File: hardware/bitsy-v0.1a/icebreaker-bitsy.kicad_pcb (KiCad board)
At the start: 4 copper layers, 38.1 x 17.8 mm, 93 parts, among them J1 Conn_01x01, J10 Conn_01x01, J11 Conn_01x01, J12 Conn_01x01, J13 Conn_01x01, J14 Jumper, J15 Jumper, J16 Jumper, J17 Jumper, J18 Jumper, J19 Jumper, J2 Conn_01x01, J20 Conn_01x01, J21 Conn_01x01, J22 Conn_01x01, J23 Conn_01x01, J24 Conn_01x01, J25 Conn_01x01, J26 Conn_01x01, J27 Conn_01x01, J28 Conn_01x01, J29 Conn_01x01, J3 Conn_01x01, J30 Conn_01x01, J31 Conn_01x01, J32 Conn_01x01, J33 Conn_01x01, J34 Conn_01x01, J35 Conn_01x01, J36 Conn_01x01, J37 Conn_01x01, J4 Conn_01x01, J41 Conn_01x01, J42 Conn_01x01, J43 Conn_01x01, J44 Conn_01x01, J45 Conn_01x01, J46 Conn_01x01, J47 Conn_01x01, J48 Conn_01x01, J49 Conn_01x01, J5 Conn_01x01, J6 Conn_01x01, J7 Conn_01x01, J8 Conn_01x01, J9 Conn_01x01, P1 pkl_USB_OTG, SW1 TACT, U2 3.3V, U3 1V2, U5 W25Q, U6 ICE5LP4K-SG48, X1 12MHz

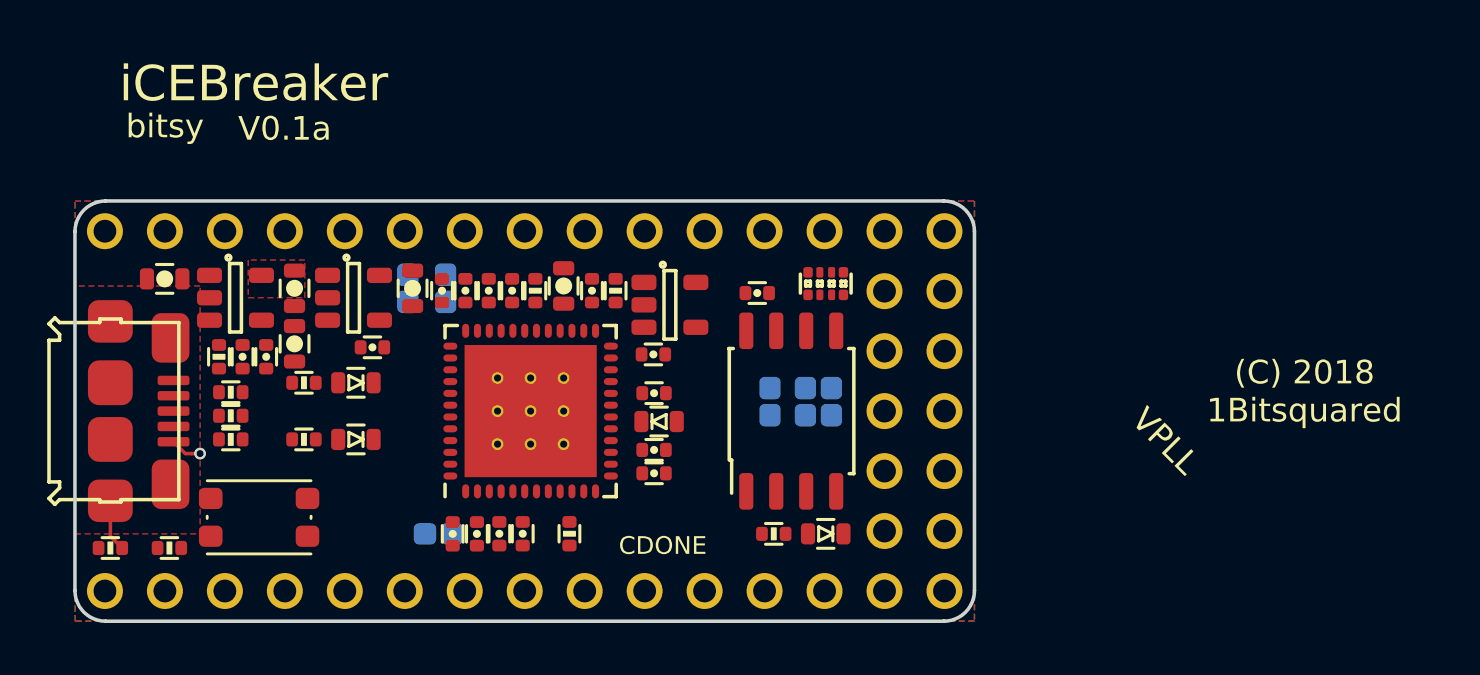
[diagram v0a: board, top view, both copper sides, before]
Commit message: Schematic cleanup and minor improvements.
Added ESD protection on the USB interface, added +5V VIN Jumper.
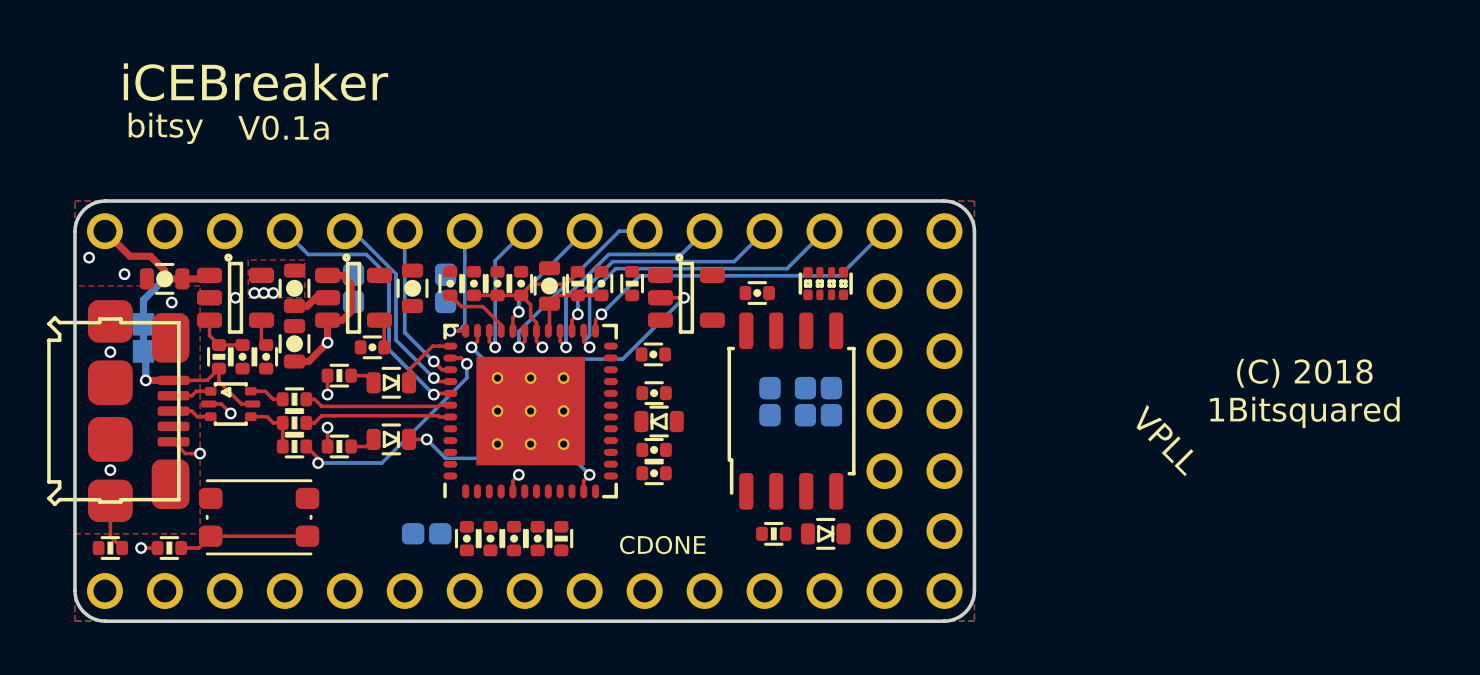
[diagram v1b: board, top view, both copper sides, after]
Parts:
- added J38: Jumper, pkl_jumpers:J_0603, B.Cu at (32.9, 44.4)
- added U1: USBLC6-2, pkl_housings_sot:SOT-666, F.Cu at (36.6, 47.2)
- P1: value pkl_USB_OTG -> USB_OTG
- moved R2 2.72 mm to (39.3, 49.0)
- moved R4 2.72 mm to (39.3, 47.0)
- moved R6 2.72 mm to (39.3, 48.0)
- moved J14 2.30 mm to (41.8, 42.3)
- moved R10 1.82 mm to (51.3, 42.1)
- moved R14 1.53 mm to (41.2, 46.0)
- moved R15 1.53 mm to (41.2, 49.0)
- moved D4 1.50 mm to (43.4, 46.3)
- moved D5 1.50 mm to (43.4, 48.7)
- moved R7 0.76 mm to (53.6, 42.1)
- moved X1 0.76 mm to (55.9, 42.7)
- moved C36 0.67 mm to (49.6, 52.9)
- moved C37 0.66 mm to (48.6, 52.9)
- moved C27 0.63 mm to (46.6, 52.9)
- moved C38 0.61 mm to (47.6, 52.9)
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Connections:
- R2 pad 2: /xUD+ -> /iUD+
- R4 pad 2: /xUD- -> /iUD-
- R6 pad 2: /xUD+ -> /iUD+
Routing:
- net +5V: track 0.00 -> 29.7 mm, vias 0 -> 3
- net /IOT_39A: track 0.00 -> 14.3 mm, vias 0 -> 1
- net /IOT_36b: track 0.00 -> 14.3 mm, vias 0 -> 1
- net /CLK: track 0.00 -> 12.1 mm, vias 0 -> 2
- net /~LED_BLU: track 0.00 -> 11.7 mm, vias 0 -> 1
- net /IOT_38B: track 0.00 -> 10.6 mm, vias 0 -> 1
- net /USB_DET: track 0.00 -> 10.1 mm, vias 0 -> 2
- net /IOT_41A: track 0.00 -> 9.96 mm, vias 0 -> 1
- net /~LEDR: track 0.00 -> 9.07 mm, vias 0 -> 2
- net /~LED_GRN: track 0.00 -> 8.75 mm, vias 0 -> 1
- net /IOT_42B: track 0.00 -> 8.56 mm, vias 0 -> 1
- net +1V2: track 0.00 -> 8.19 mm, vias 0 -> 2
- net /~LED_RED: track 0.00 -> 6.87 mm, vias 0 -> 1
- net /IOT_44B: track 0.00 -> 6.42 mm, vias 0 -> 1
- net /USB_P: track 0.00 -> 6.24 mm
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- added copper zone on In2.Cu, net +1V2
- added copper zone on In1.Cu, net /shield

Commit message: First shot at fully routing the board! :D
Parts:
- moved REF** 45.2 mm to (41.6, 47.4), turned to 90 degrees
- moved C31 5.34 mm to (54.8, 44.8)
- moved C4 2.22 mm to (56.7, 44.8)
- moved C29 0.98 mm to (54.8, 48.2)
- moved C35 0.98 mm to (54.8, 45.8)
- moved D2 0.98 mm to (55.0, 47.0)
- moved R11 0.81 mm to (61.0, 42.0)
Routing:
- net +3V3: track 5.22 -> 41.4 mm, vias 7 -> 19
- net /FLASH_MISO/IO1: track 0.00 -> 24.9 mm, vias 0 -> 3
- net /FLASH_~WP~/IO2: track 0.00 -> 24.6 mm, vias 0 -> 2
- net /FLASH_MOSI/IO0: track 0.00 -> 22.3 mm, vias 0 -> 3
- net /iCE_SS_B: track 0.00 -> 21.4 mm, vias 0 -> 3
- net /IOB_29B: track 0.00 -> 20.4 mm, vias 0 -> 1
- net +1V2: track 8.19 -> 28.1 mm, vias 2 -> 4
- net /iCE_CDONE: track 0.00 -> 19.8 mm, vias 0 -> 2
- net /FLASH_~HLD~/~RST~/IO3: track 0.00 -> 19.6 mm
- net /IOB_25B_G3: track 0.00 -> 18.8 mm, vias 0 -> 1
- net /iCE_CRESET: track 0.00 -> 18.6 mm, vias 0 -> 1
- net /IOB_31B: track 0.00 -> 18.2 mm, vias 0 -> 2
- net /IOB_3B_G6: track 0.00 -> 17.9 mm, vias 0 -> 1
- net /iCE_SCK: track 0.00 -> 17.6 mm, vias 0 -> 3
- net /IOT_37A: track 0.00 -> 16.7 mm, vias 0 -> 1
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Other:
- board text added: "1"
- board text added: "18"
- board text added: "19"
- board text added: "1Bitsquared (C) 2018"
- board text added: "1Bitsquared 2018"
- board text added: "1V2"
- board text added: "2"
- board text added: "20"
- board text added: "22"
- board text added: "23"
- board text added: "24"
- board text added: "25"
- board text added: "27"
- board text added: "3"
- board text added: "3V3"
- board text added: "4"
- board text added: "5"
- board text added: "6"
- board text added: "7"
- board text added: "8"
- board text added: "C"
- board text added: "CC-BY-SA"
- board text added: "D"
- board text added: "G"
- board text added: "GND"
- board text added: "I"
- board text added: "K"
- board text added: "N"
- board text added: "O"
- board text added: "PROG"
- board text added: "R"
- board text added: "S"
- board text added: "User Button"
- board text added: "VIN"
- board text removed: "(C) 2018 1Bitsquared"
- board text removed: "1Bitsquared"
- board text removed: "VPLL"

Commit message: Adjusted USB resistor values based on Luke Valenty suggestions.
Thanks @tinyfpga ! :D
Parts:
- R2: value 15k -> 1k5
- R4, R6: value 68E -> 22E
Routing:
- net +3V3: track 41.4 -> 42.9 mm
- net /iCE_SCK: track 17.6 -> 18.3 mm
- net /FLASH_MOSI/IO0: track 22.3 -> 23.0 mm
- net /iCE_SS_B: track 21.4 -> 22.1 mm
- net GND: vias 9 -> 17

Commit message: Minor cleanups, ready to order prototypes! :D
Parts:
- moved C24 0.10 mm to (50.1, 42.3)
- turned C29 to 0 degrees
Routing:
- net +3V3: track 42.9 -> 43.6 mm
- net GND: vias 17 -> 18
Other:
- rule trace_min: 0.149 -> 0.15
- board text removed: "VCCIO0&1"
